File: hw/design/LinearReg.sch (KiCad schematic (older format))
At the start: 12 parts

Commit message: aux output, documentation
finished aux output circuit, updated a lot of documentation, added datasheets
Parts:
- C?: VRating 10V -> 16V
- R?: value 205k -> 270k; footprint Resistor_SMD:R_0603_1608Metric -> Resistor_SMD:R_1206_3216Metric_Pad1.42x1.75mm_HandSolder; Size (none) -> 1206
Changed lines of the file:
@@
 $Descr A4 11693 8268
 encoding utf-8
-Sheet 2 6
+Sheet 2 7
 Title ""
 Date ""
@@
 U 1 1 5E99EF91
 P 7000 2550
-F 0 "R?" H 7068 2596 50  0000 L CNN
-F 1 "205k" H 7068 2505 50  0000 L CNN
-F 2 "Resistor_SMD:R_0603_1608Metric" V 7040 2540 50  0001 C CNN
+F 0 "R?" H 7050 2600 50  0000 L CNN
+F 1 "270k" H 7050 2500 50  0000 L CNN
+F 2 "Resistor_SMD:R_1206_3216Metric_Pad1.42x1.75mm_HandSolder" V 7040 2540 50  0001 C CNN
 F 3 "~" H 7000 2550 50  0001 C CNN
+F 4 "1206" H 7050 2400 50  0000 L CNN "Size"
 	1    7000 2550
 	1    0    0    -1
@@
 F 2 "Capacitor_SMD:C_0603_1608Metric" H 5138 3050 50  0001 C CNN
 F 3 "~" H 5100 3200 50  0001 C CNN
-F 4 "10V" H 5250 3100 50  0000 L CNN "VRating"
-F 5 "0402" H 5250 3000 50  0000 L CNN "Size"
+F 4 "16V" H 5250 3100 50  0001 L CNN "VRating"
+F 5 "0402" H 5250 3000 50  0001 L CNN "Size"
 	1    5100 3200
 	-1   0    0    -1

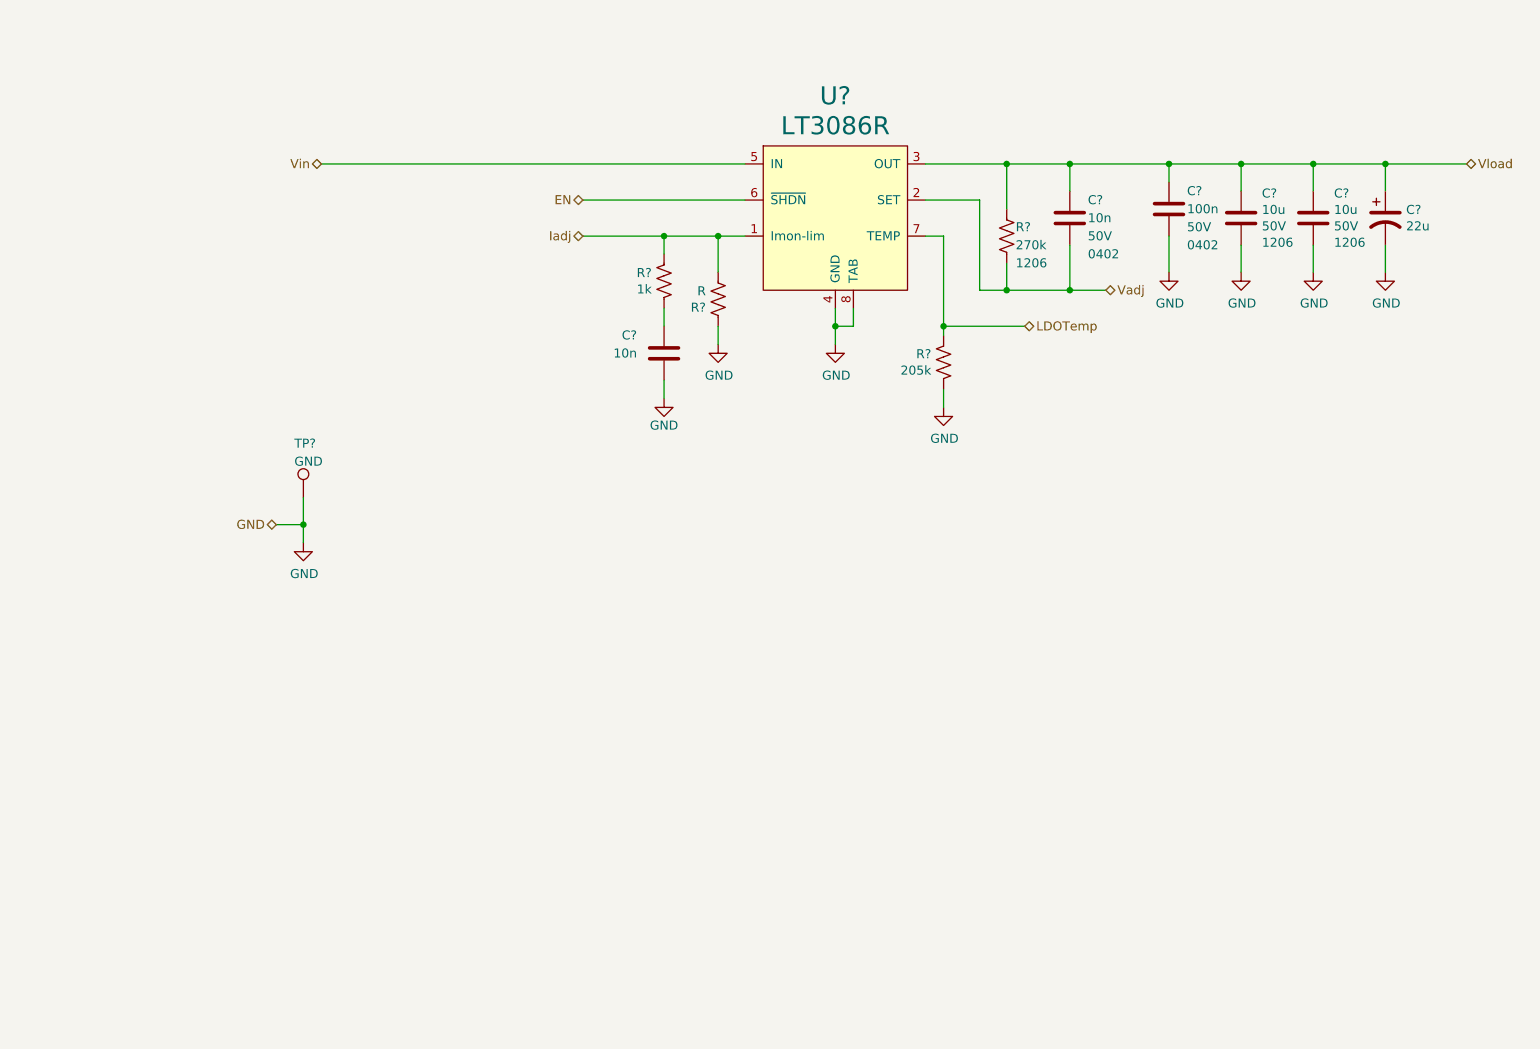
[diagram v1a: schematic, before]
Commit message: reworked adjusters
new V/I adjustment scheme; modified LDO circuit to match
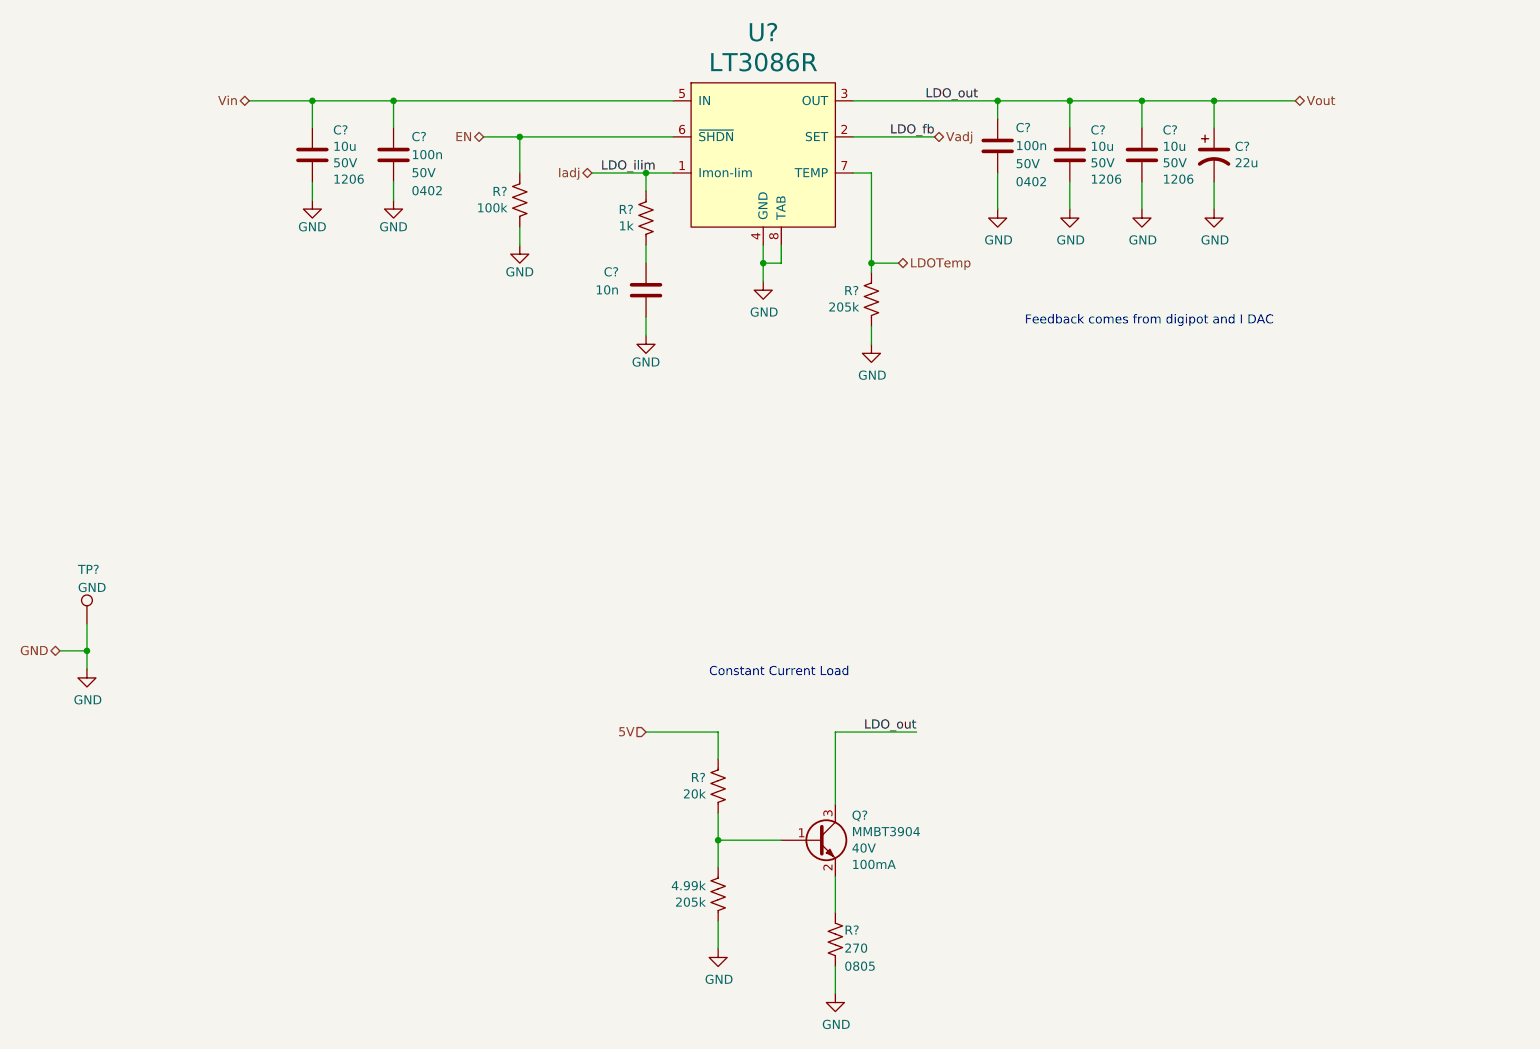
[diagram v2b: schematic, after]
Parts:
- removed C?: 10n, Capacitor_SMD:C_0603_1608Metric, symbol Device:C
- removed R?: 270k, Resistor_SMD:R_1206_3216Metric_Pad1.42x1.75mm_HandSolder, symbol Device:R_US
- removed R?: R, Resistor_SMD:R_0603_1608Metric, symbol Device:R_US
- added 4.99k: 205k, Resistor_SMD:R_0603_1608Metric, symbol Device:R_US
- added C?: 10u, Capacitor_SMD:C_1206_3216Metric_Pad1.42x1.75mm_HandSolder, symbol Device:C
- added C?: 100n, Capacitor_SMD:C_0603_1608Metric, symbol Device:C
- added Q?: MMBT3904, Package_TO_SOT_SMD:SOT-23, symbol Transistor_BJT:MMBT3904
- added R?: 100k, Resistor_SMD:R_0603_1608Metric, symbol Device:R_US
- added R?: 270, Resistor_SMD:R_0805_2012Metric_Pad1.15x1.40mm_HandSolder, symbol Device:R_US
- added R?: 20k, Resistor_SMD:R_0603_1608Metric, symbol Device:R_US
- C? (x2): footprint Capacitor_SMD:C_0805_2012Metric_Pad1.15x1.40mm_HandSolder -> Capacitor_SMD:C_1206_3216Metric_Pad1.42x1.75mm_HandSolder
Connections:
- net EN: now also R?.1
- net GND: now also 4.99k.2, C?.2, C?.2, R?.2, R?.2
- net Vin: now also C?.1, C?.1
- net Vload renamed Vout
- net Vout: now also Q?.3 (C)
- new net: 4.99k.1, Q?.1 (B), R?.2
- new net: Q?.2 (E), R?.1
- new net 5V: R?.1
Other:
- note added: "Constant Current Load"
- note added: "Feedback comes from digipot and I DAC"
- moved on the sheet: C?, R?, TP?, U?

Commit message: sims, new devices, code started
made some simulations & calculations, started working on code (moved devices into individual header files), new devices chosen in library
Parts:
- removed C?: 100n, Capacitor_SMD:C_0603_1608Metric, symbol Device:C
- added C?: C_Feedthrough, symbol Device:C_Feedthrough
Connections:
- net GND: now also C?.2
- net Vout: now also C?.3; no longer U?.3 (OUT)
- new net LDO_O: C?.1, U?.3 (OUT)
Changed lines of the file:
@@
 Wire Wire Line
 	7350 1950 7350 1800
-Connection ~ 7350 1800
 Wire Wire Line
 	7350 1800 7750 1800
@@
 LDOTemp
 $Comp
-L Device:C C?
-U 1 1 5ECC6C16
-P 6950 2050
-AR Path="/5E84FADE/5ECC6C16" Ref="C?"  Part="1"
-AR Path="/5E917C1A/5ECC6C16" Ref="C?"  Part="1"
-F 0 "C?" H 7050 2150 50  0000 L CNN
-F 1 "100n" H 7050 2050 50  0000 L CNN
-F 2 "Capacitor_SMD:C_0603_1608Metric" H 6988 1900 50  0001 C CNN
-F 3 "~" H 6950 2050 50  0001 C CNN
-F 4 "Murata_GRM155R61H104KE19D" H 6950 2050 50  0001 C CNN "MfrNum"
-F 5 "50V" H 7050 1950 50  0000 L CNN "VRating"
-F 6 "0402" H 7050 1850 50  0000 L CNN "Size"
-	1    6950 2050
-	1    0    0    -1
-$EndComp
-$Comp
 L power:GND #PWR?
 U 1 1 5ECC6C1D
@@
 	1    0    0    -1
 $EndComp
-Wire Wire Line
-	6950 2400 6950 2200
-Wire Wire Line
-	6950 1900 6950 1800
-Connection ~ 6950 1800
-Wire Wire Line
-	6950 1800 7350 1800
 $Comp
 L Device:R_US R?
@@
 	1900 4700 1900 4850
 Connection ~ 1900 4850
-Text Label 6550 1800 0    50   ~ 0
-LDO_out
-Wire Wire Line
-	6150 1800 6950 1800
 Wire Wire Line
 	5000 2200 5150 2200
@@
 Text Notes 7100 3050 0    50   ~ 0
 Feedback comes from digipot and I DAC
+$Comp
+L Device:C_Feedthrough C?
+U 1 1 6067EC07
+P 6950 1900
+F 0 "C?" H 6950 2205 50  0000 C CNN
+F 1 "C_Feedthrough" H 6950 2114 50  0000 C CNN
+F 2 "" V 6950 1900 50  0001 C CNN
+F 3 "~" V 6950 1900 50  0001 C CNN
+	1    6950 1900
+	1    0    0    -1
+$EndComp
+Wire Wire Line
+	6950 2000 6950 2400
+Wire Wire Line
+	6750 1800 6150 1800
+Wire Wire Line
+	7150 1800 7350 1800
+Connection ~ 7350 1800
+Text Label 6250 1800 0    50   ~ 0
+LDO_O
+Text Label 7550 1800 0    50   ~ 0
+LDO_out
 $EndSCHEMATC
